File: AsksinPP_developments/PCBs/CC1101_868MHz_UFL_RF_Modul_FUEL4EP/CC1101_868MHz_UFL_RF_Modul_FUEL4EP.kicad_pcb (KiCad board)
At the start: 2 copper layers, 19 x 13 mm, 40 parts, among them U1 CC1101RGPR, Y1 Crystal 26MHz

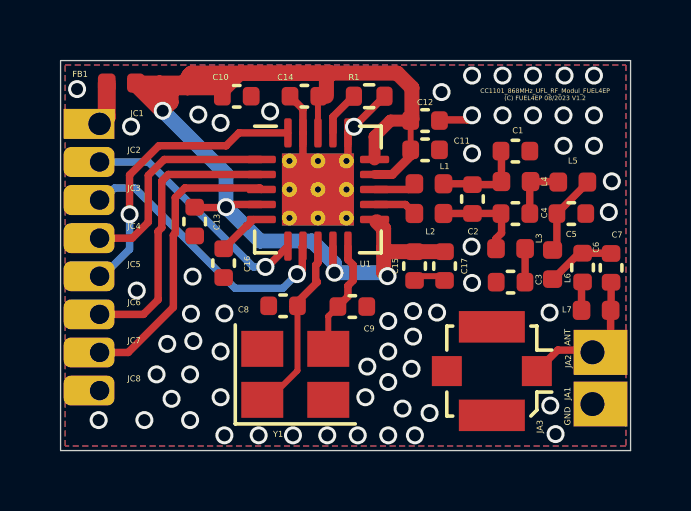
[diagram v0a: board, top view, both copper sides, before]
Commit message: PCBs: CC1101_868MHz_RF_Modul_FUEL4EP, CC1101_868MHz_UFL_RF_Modul_FUEL4EP: update of silkscreen texts
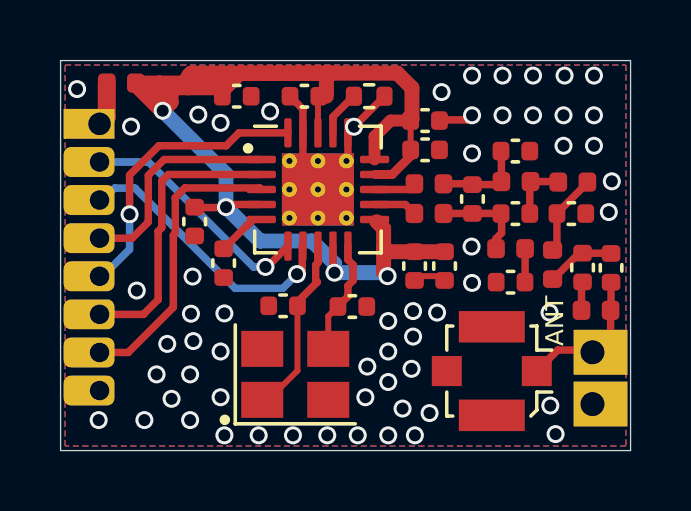
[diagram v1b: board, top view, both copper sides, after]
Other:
- board text added: "CC1101_868MHz_UFL_ RF_Modul_FUEL4EP V1.3 (C) FUEL4EP 09/2023"
- board text added: "JLCJLCJLCJLC"
- board text removed: "CC1101_868MHz_UFL_RF_Modul_FUEL4EP (C) FUEL4EP 08/2023 V1.2"
- board text removed: "GND"

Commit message: PCBs: CC1101_868MHz_UFL_RF_Modul_FUEL4EP: derivated from CC1101_868MHz_RF_Modul_FUEL4EP with improved decoupling capacitor return paths
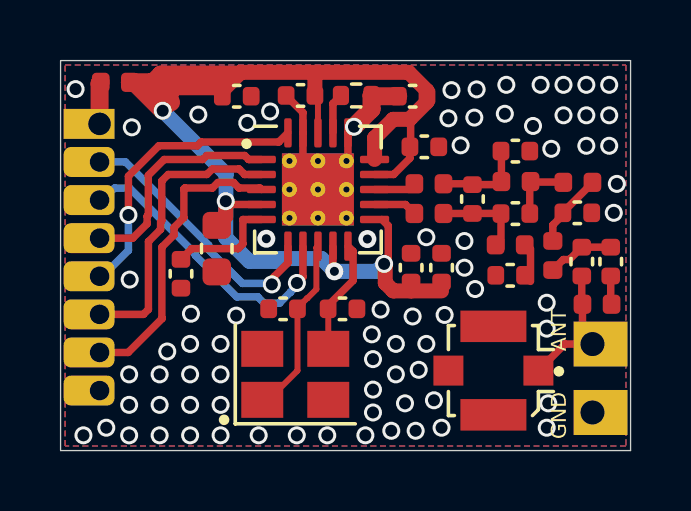
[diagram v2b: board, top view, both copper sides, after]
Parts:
- C13: footprint Capacitor_SMD:C_0402_1005Metric -> Capacitor_SMD:C_0603_1608Metric
- C6: value 47pF -> 12pF
- C7: value 12pF -> 47pF
- JA1: value GND -> Ant.
- JA2: value Ant. -> GND
- moved JA2 2.00 mm to (19.0, -1.27)
- moved JA1 2.00 mm to (19.0, -3.55)
- moved C16 1.47 mm to (4.01, -5.89)
- moved C13 1.17 mm to (5.21, -6.73)
- moved C12 0.91 mm to (11.7, -11.8), turned to 180 degrees
- moved R1 0.43 mm to (9.86, -11.8)
- moved C9 0.34 mm to (9.40, -4.72)
- moved L6 0.30 mm to (16.4, -6.50)
- moved C3 0.23 mm to (15.0, -5.84)
- moved C7 0.21 mm to (18.3, -6.30)
- moved L7 0.20 mm to (17.9, -4.88), turned to 180 degrees
- moved FB1 0.20 mm to (1.82, -12.3)
- moved C6 0.20 mm to (17.4, -6.30)
- moved C5 0.20 mm to (17.2, -7.93)
- moved L5 0.17 mm to (17.2, -8.94)
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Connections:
- JA1 pad 1: GND -> Net-(C6-Pad1)
- JA2 pad 1: Net-(C7-Pad1) -> GND
- JA3 pad 1: Net-(C7-Pad1) -> Net-(C6-Pad1)
- L7 pad 1: Net-(C6-Pad1) -> Net-(C7-Pad1)
- L7 pad 2: Net-(C7-Pad1) -> Net-(C6-Pad1)
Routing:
- net Net-(C7-Pad1): track 4.12 -> 0.91 mm
- net Net-(C6-Pad1): track 0.91 -> 4.08 mm
- net Net-(C16-Pad1): track 1.40 -> 3.71 mm
- net GND: track 7.22 -> 5.83 mm, vias 59 -> 76
- net VDDA: track 44.4 -> 45.3 mm
- net /GDO0: track 7.92 -> 8.78 mm
- net /~{CS}: track 9.24 -> 9.82 mm
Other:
- board text added: "CC1101_868MHz_UFL RF_Modul_FUEL4EP V1.4 (C) FUEL4EP 09/2023"
- board text added: "GND"
- board text removed: "CC1101_868MHz_UFL_ RF_Modul_FUEL4EP V1.3 (C) FUEL4EP 09/2023"

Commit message: PCBs: CC1101_868MHz_RF_Modul_FUEL4EP and CC1101_868MHz_UFL_RF_Modul_FUEL4EP: Reduction of parasitic capaitance of oscillator layout; use 1% CoG capacitors for oscillator
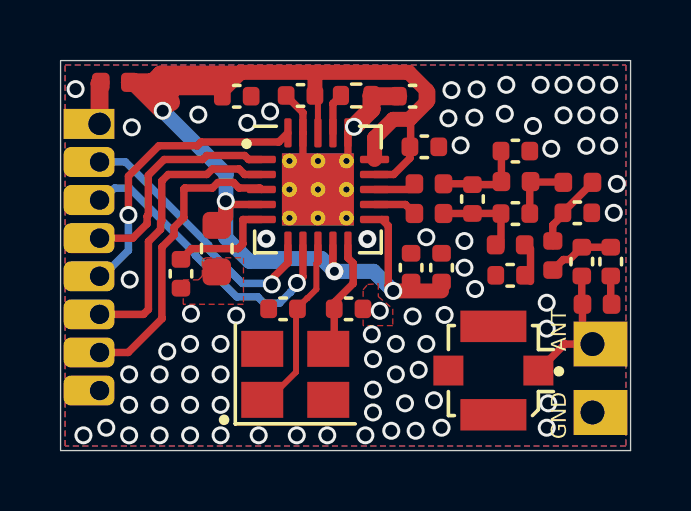
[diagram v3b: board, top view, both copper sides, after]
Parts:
- moved C9 0.20 mm to (9.60, -4.72)
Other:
- board text added: "CC1101_868MHz_UFL RF_Modul_FUEL4EP V1.5 (C) FUEL4EP 09/2023"
- board text removed: "CC1101_868MHz_UFL RF_Modul_FUEL4EP V1.4 (C) FUEL4EP 09/2023"
